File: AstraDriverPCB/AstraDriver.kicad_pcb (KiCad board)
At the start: 4 copper layers, 102 x 96 mm, 52 parts, among them CN2 JST VH 2 PIN, CN3 JST VH 2 PIN, CN4 JST VH 2 PIN, CN5 JST VH 2 PIN, CN6 JST VH 8 PIN, U1 LED2001PHR, U2 LED2001PHR, U3 LED2001PHR, U4 LED2001PHR

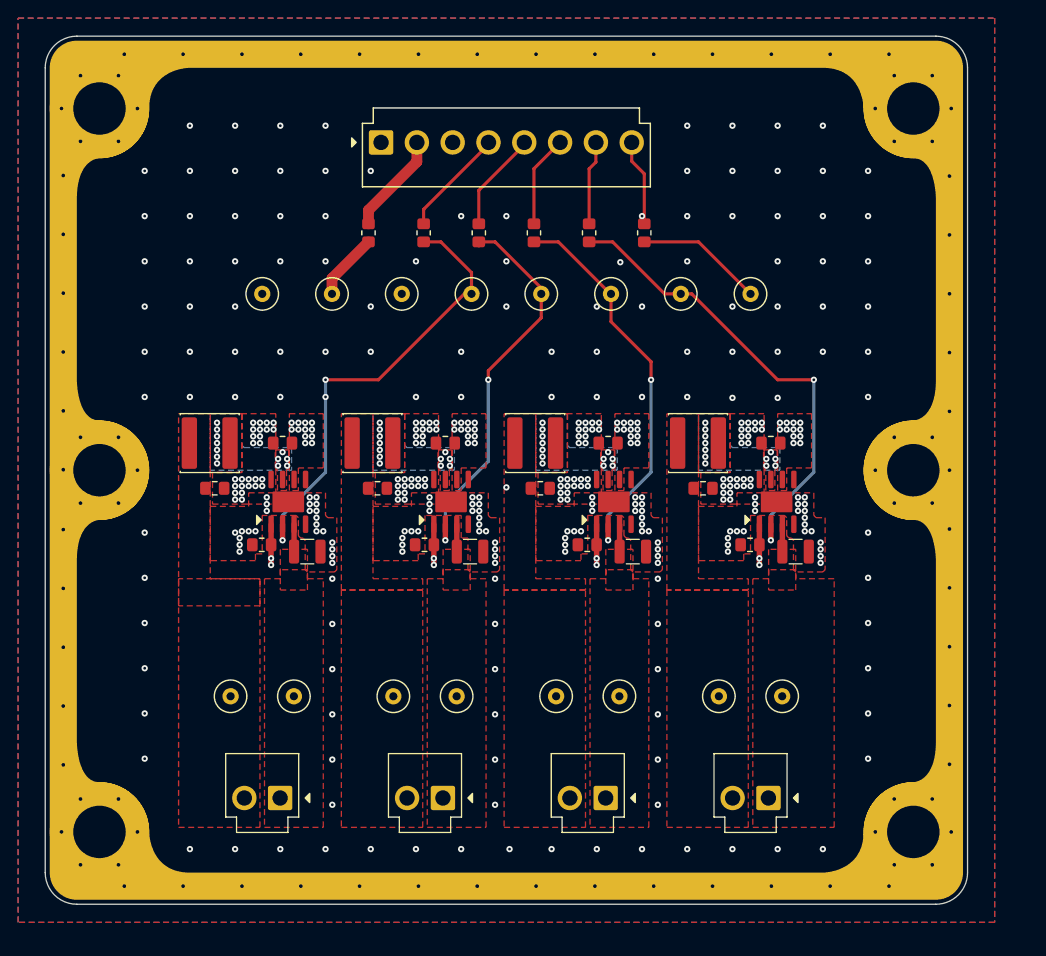
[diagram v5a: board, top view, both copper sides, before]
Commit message: Added extra caps, cleanup
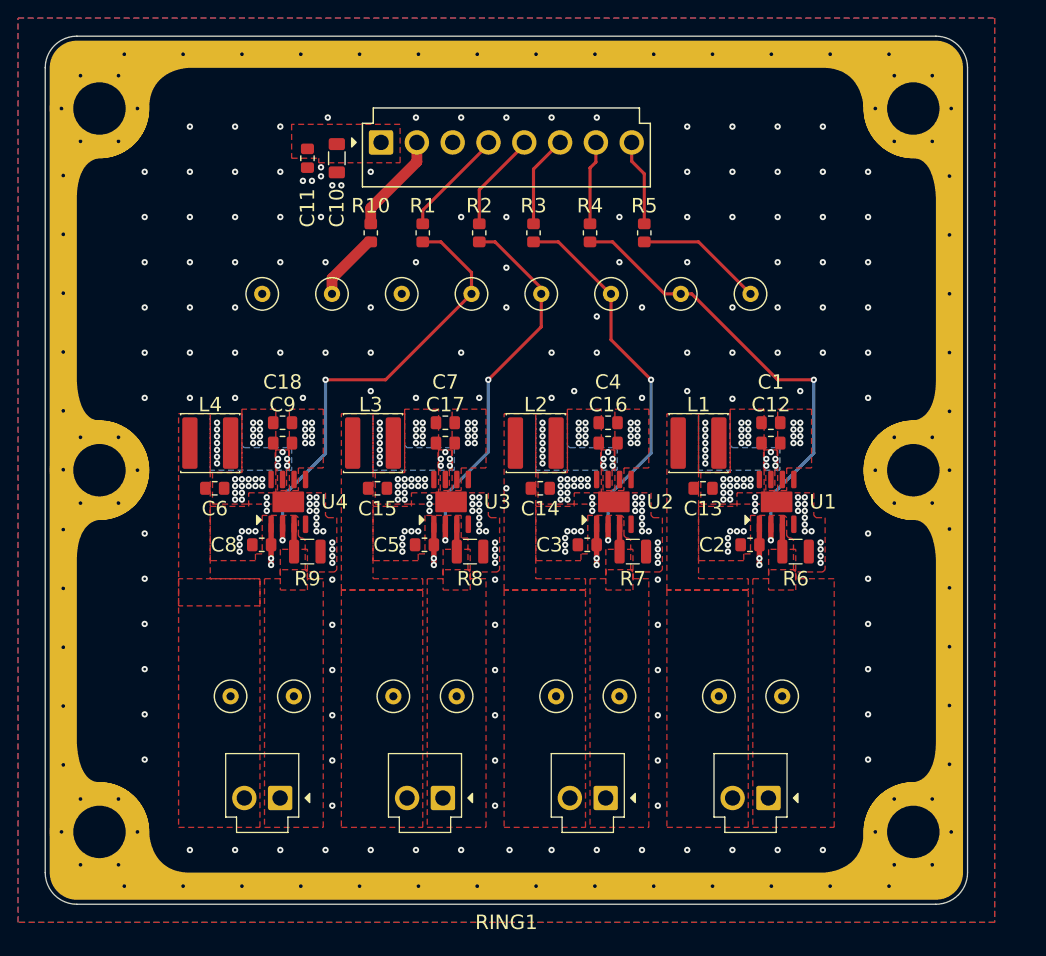
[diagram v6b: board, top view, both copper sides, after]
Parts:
- added C10: 100u, LiveAstra:C_1206_3216Metric_Pad1.33x1.80mm_HandSolder, F.Cu at (129.8, 70.5)
- added C11: DNP, LiveAstra:C_DNP_0805_2012Metric_Pad1.18x1.45mm_HandSolder, F.Cu at (126.5, 70.5)
- added C12: DNP, LiveAstra:C_DNP_0805_2012Metric_Pad1.18x1.45mm_HandSolder, F.Cu at (177.8, 99.8)
- added C16: DNP, LiveAstra:C_DNP_0805_2012Metric_Pad1.18x1.45mm_HandSolder, F.Cu at (159.8, 99.8)
- added C17: DNP, LiveAstra:C_DNP_0805_2012Metric_Pad1.18x1.45mm_HandSolder, F.Cu at (141.8, 99.8)
- added C18: DNP, LiveAstra:C_DNP_0805_2012Metric_Pad1.18x1.45mm_HandSolder, F.Cu at (123.8, 99.8)
- moved R10 0.25 mm to (133.5, 78.8)
- moved R1 0.10 mm to (139.2, 78.8)
- moved R4 0.10 mm to (157.8, 78.8)
- moved L1 0.06 mm to (169.8, 102.0)
- moved L2 0.06 mm to (151.8, 102.0)
- moved L3 0.06 mm to (133.8, 102.0)
- moved L4 0.06 mm to (115.8, 102.0)
- moved R2 0.05 mm to (145.5, 78.8)
- moved R3 0.05 mm to (151.5, 78.8)
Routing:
- net GND: vias 326 -> 319
- net +5V: vias 56 -> 40

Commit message: Finished silkscreen and board
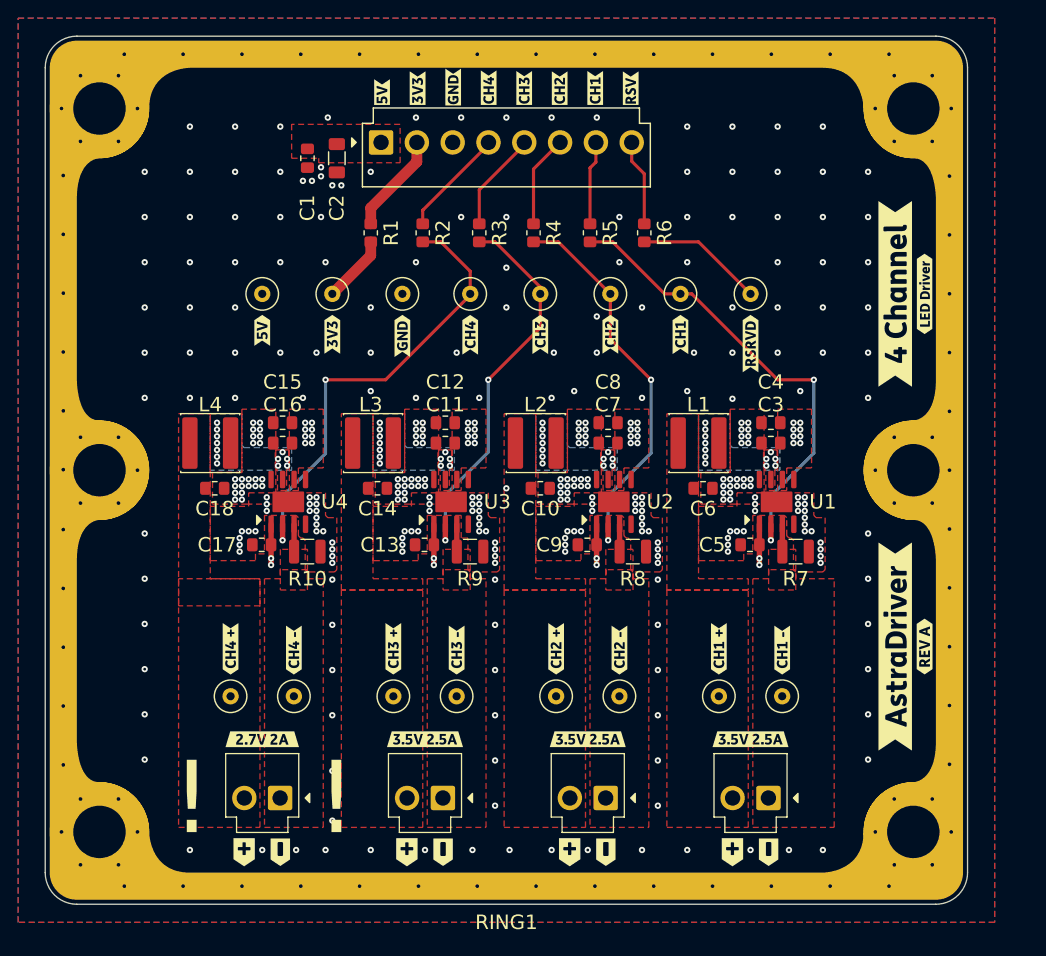
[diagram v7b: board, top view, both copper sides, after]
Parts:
- added kibuzzard-67263D4A: G***, kibuzzard-67263D4A, F.Cu at (134.8, 63.2)
- added kibuzzard-67263D55: G***, kibuzzard-67263D55, F.Cu at (138.7, 62.7)
- added kibuzzard-67263D65: G***, kibuzzard-67263D65, F.Cu at (142.6, 62.6)
- added kibuzzard-67263D6B: G***, kibuzzard-67263D6B, F.Cu at (146.5, 62.7)
- added kibuzzard-67263D70: G***, kibuzzard-67263D70, F.Cu at (150.5, 62.7)
- added kibuzzard-67263D73: G***, kibuzzard-67263D73, F.Cu at (154.4, 62.7)
- added kibuzzard-67263D79: G***, kibuzzard-67263D79, F.Cu at (158.3, 62.7)
- added kibuzzard-67263D89: G***, kibuzzard-67263D89, F.Cu at (162.2, 62.8)
- added kibuzzard-67263EBF: G***, kibuzzard-67263EBF, F.Cu at (121.5, 89.5)
- added kibuzzard-67263F1F: G***, kibuzzard-67263F1F, F.Cu at (144.5, 90.0)
- added kibuzzard-67263F2B: G***, kibuzzard-67263F2B, F.Cu at (175.5, 91.0)
- added kibuzzard-67263F35: G***, kibuzzard-67263F35, F.Cu at (167.8, 90.0)
- added kibuzzard-67263F3C: G***, kibuzzard-67263F3C, F.Cu at (160.0, 90.0)
- added kibuzzard-67263F3F: G***, kibuzzard-67263F3F, F.Cu at (152.2, 90.0)
- added kibuzzard-67263F87: G***, kibuzzard-67263F87, F.Cu at (129.2, 90.0)
- added kibuzzard-67263F8C: G***, kibuzzard-67263F8C, F.Cu at (137.0, 90.2)
- added kibuzzard-6726414E: G***, kibuzzard-6726414E, F.Cu at (155.5, 147.2)
- added kibuzzard-6726414E: G***, kibuzzard-6726414E, F.Cu at (173.5, 147.2)
- added kibuzzard-6726414E: G***, kibuzzard-6726414E, F.Cu at (119.5, 147.2)
- added kibuzzard-6726414E: G***, kibuzzard-6726414E, F.Cu at (137.5, 147.2)
- added kibuzzard-67264157: G***, kibuzzard-67264157, F.Cu at (177.5, 147.2)
- added kibuzzard-67264157: G***, kibuzzard-67264157, F.Cu at (141.5, 147.2)
- added kibuzzard-67264157: G***, kibuzzard-67264157, F.Cu at (123.5, 147.2)
- added kibuzzard-67264157: G***, kibuzzard-67264157, F.Cu at (159.5, 147.2)
- added kibuzzard-672641C9: G***, kibuzzard-672641C9, F.Cu at (125.0, 124.9)
- added kibuzzard-672641CE: G***, kibuzzard-672641CE, F.Cu at (118.0, 124.8)
- added kibuzzard-67264513: G***, kibuzzard-67264513, F.Cu at (179.0, 124.9)
- added kibuzzard-6726451B: G***, kibuzzard-6726451B, F.Cu at (172.0, 124.8)
- added kibuzzard-67264761: G***, kibuzzard-67264761, F.Cu at (136.0, 124.8)
- added kibuzzard-6726476F: G***, kibuzzard-6726476F, F.Cu at (143.0, 124.9)
- added kibuzzard-67264778: G***, kibuzzard-67264778, F.Cu at (154.0, 124.8)
- added kibuzzard-6726477C: G***, kibuzzard-6726477C, F.Cu at (161.0, 124.9)
- added kibuzzard-672647E1: G***, kibuzzard-672647E1, F.Cu at (121.5, 134.8)
- added kibuzzard-6726481C: G***, kibuzzard-6726481C, F.Cu at (175.5, 134.8)
- added kibuzzard-6726481C: G***, kibuzzard-6726481C, F.Cu at (157.5, 134.8)
- added kibuzzard-6726481C: G***, kibuzzard-6726481C, F.Cu at (139.5, 134.8)
- added kibuzzard-67264EAC: G***, kibuzzard-67264EAC, F.Cu at (191.5, 124.5)
- added kibuzzard-67264F3E: G***, kibuzzard-67264F3E, F.Cu at (191.5, 85.5)
- added kibuzzard-67264F60: G***, kibuzzard-67264F60, F.Cu at (194.8, 124.5)
- added kibuzzard-67264F65: G***, kibuzzard-67264F65, F.Cu at (194.8, 85.5)
- moved TP4 0.14 mm to (144.5, 85.5)
- moved TP5 0.11 mm to (152.2, 85.5)
- moved TP3 0.07 mm to (137.0, 85.5)
- moved TP6 0.07 mm to (160.0, 85.5)
- renumbered C11 to C1, C14 to C10, C17 to C11, C7 to C12, C5 to C13, C15 to C14, C18 to C15, C9 to C16, C8 to C17, C6 to C18, C10 to C2, C12 to C3, C1 to C4, C2 to C5, C13 to C6, C16 to C7, C4 to C8, C3 to C9, CN6 to CN1, R10 to R1, R9 to R10, R1 to R2, R2 to R3, R3 to R4, R4 to R5, R5 to R6, R6 to R7, R7 to R8, R8 to R9
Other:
- board text added: "!"

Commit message: DFM fixes
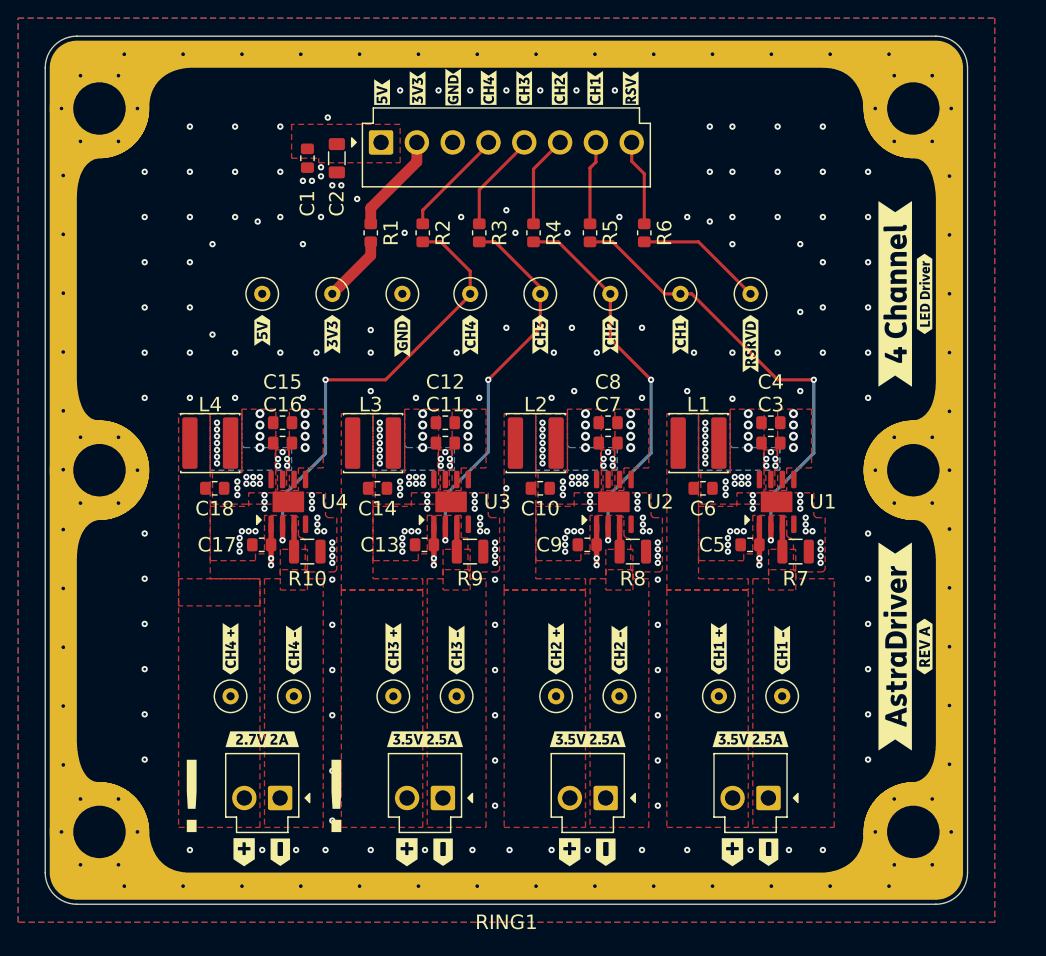
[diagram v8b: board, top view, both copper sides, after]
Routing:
- net +5V: track 18.0 -> 18.1 mm, vias 40 -> 24
- net GND: vias 319 -> 273
